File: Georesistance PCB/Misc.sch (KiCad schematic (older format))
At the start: 20 parts, among them J1 Screw_Terminal_01x04, J2 Screw_Terminal_01x02, J3 Conn_01x11_Male, U1 RS8554, U5 TXS0108EPWR, U7 ADS1115IDGS

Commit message: Actually fixed the schematic
Hopefully for the last time
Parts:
- renumbered U7 to U6
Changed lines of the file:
@@
 	9650 1500 9350 1500
 $Comp
-L Analog_ADC:ADS1115IDGS U7
+L Analog_ADC:ADS1115IDGS U6
 U 1 1 613ED4C8
 P 9350 2000
-F 0 "U7" H 9350 2681 50  0001 C CNN
+F 0 "U6" H 9350 2681 50  0001 C CNN
 F 1 "ADS1115IDGS" H 9350 2590 50  0001 C CNN
 F 2 "Package_SO:TSSOP-10_3x3mm_P0.5mm" H 9350 1500 50  0001 C CNN

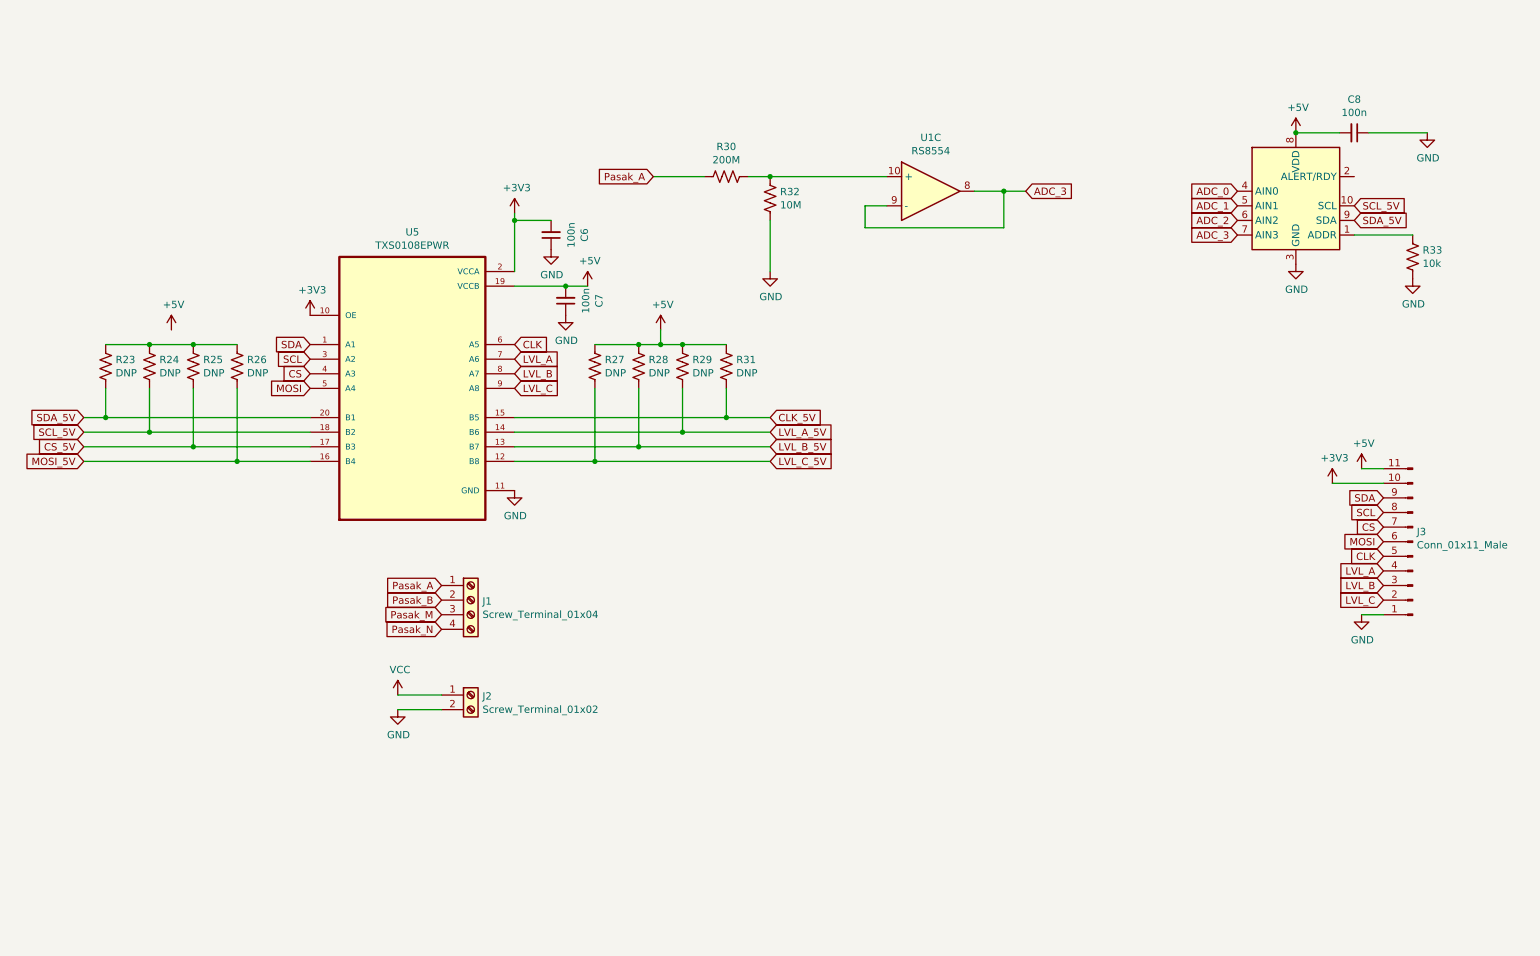
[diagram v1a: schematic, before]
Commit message: Added the PCB layout and simplified schematic
deleted jumper, and fixed misconnection
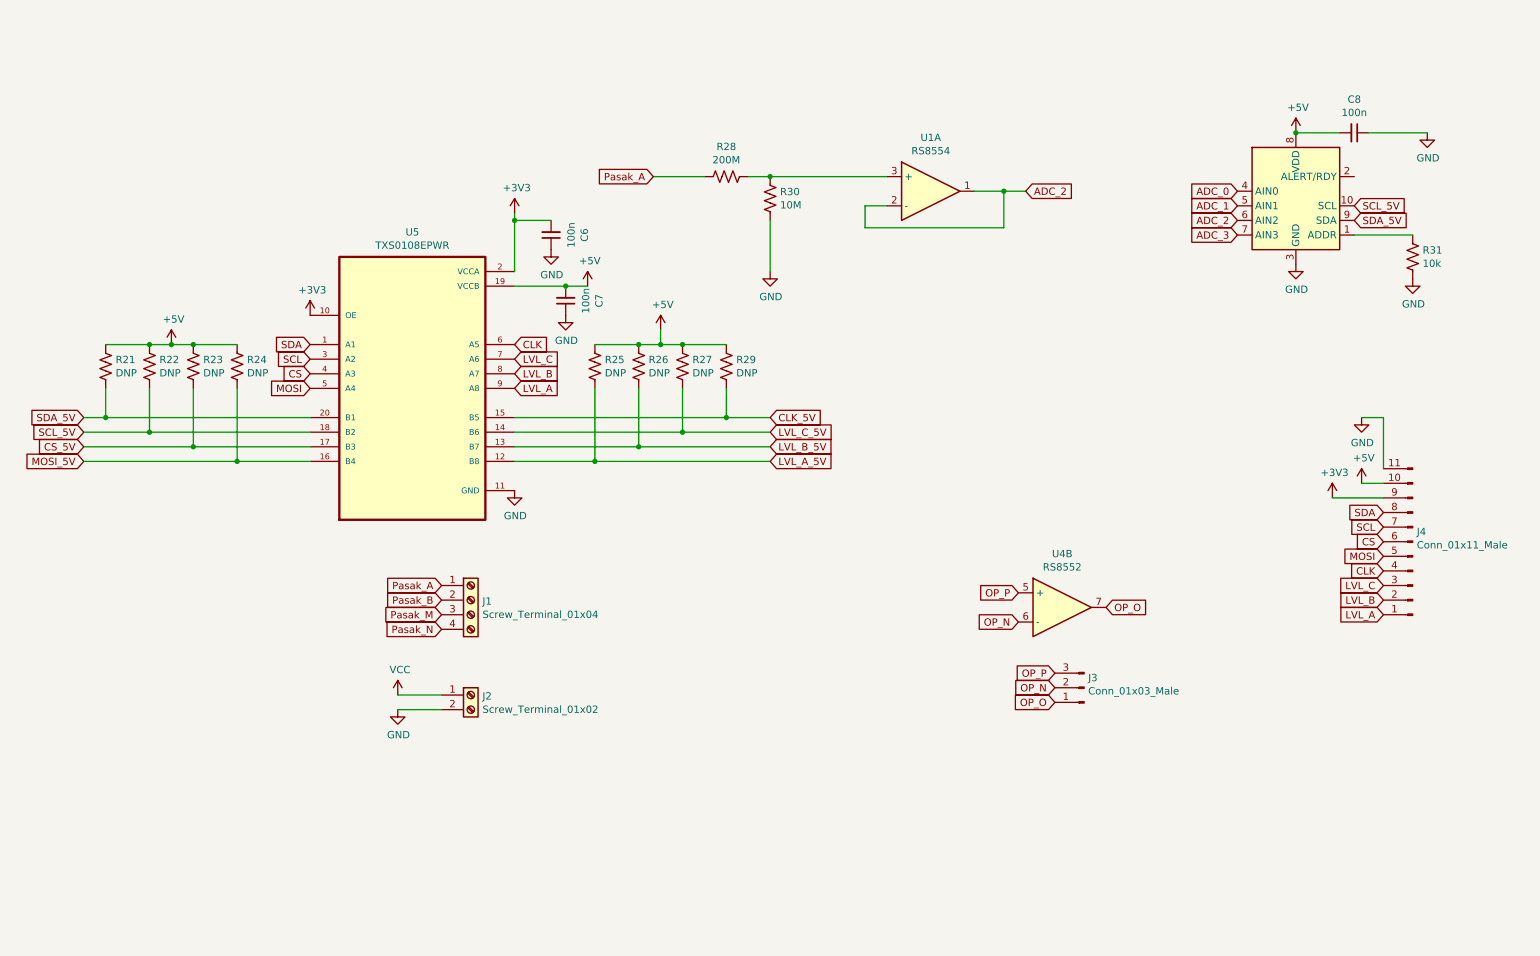
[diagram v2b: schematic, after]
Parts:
- added J3: Conn_01x03_Male, Connector_PinSocket_2.54mm:PinSocket_1x03_P2.54mm_Vertical, symbol Connector:Conn_01x03_Male
- added U4: RS8552, Package_SO:MSOP-8_3x3mm_P0.65mm, symbol Device:Opamp_Dual_Generic
- renumbered J3 to J4, R23 to R21, R24 to R22, R25 to R23, R26 to R24, R27 to R25, R28 to R26, R29 to R27, R30 to R28, R31 to R29, R32 to R30, R33 to R31
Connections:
- net +3V3: now also J4.9 (Pin_9); no longer J4.10 (Pin_10)
- net +5V: now also J4.10 (Pin_10), R21.1, R22.1, R23.1, R24.1; no longer J4.11 (Pin_11)
- net ADC_2: now also U1.1, U1.2 (-)
- net ADC_3: no longer U1.8, U1.9 (-)
- net CLK: now also J4.4 (Pin_4); no longer J4.5 (Pin_5)
- net CS: now also J4.6 (Pin_6); no longer J4.7 (Pin_7)
- net GND: now also J4.11 (Pin_11); no longer J4.1 (Pin_1)
- net LVL_A: now also J4.1 (Pin_1), U5.9 (A8); no longer J4.4 (Pin_4), U5.7 (A6)
- net LVL_A_5V: now also R25.2, U5.12 (B8); no longer R27.2, U5.14 (B6)
- net LVL_B: now also J4.2 (Pin_2); no longer J4.3 (Pin_3)
- net LVL_C: now also J4.3 (Pin_3), U5.7 (A6); no longer J4.2 (Pin_2), U5.9 (A8)
- net LVL_C_5V: now also R27.2, U5.14 (B6); no longer R25.2, U5.12 (B8)
- net MOSI: now also J4.5 (Pin_5); no longer J4.6 (Pin_6)
- net SCL: now also J4.7 (Pin_7); no longer J4.8 (Pin_8)
- net SDA: now also J4.8 (Pin_8); no longer J4.9 (Pin_9)
- net at R28.1, R30.2: now also U1.3 (+); no longer U1.10 (+)
- new net OP_N: J3.2 (Pin_2), U4.6 (-)
- new net OP_O: J3.1 (Pin_1), U4.7
- new net OP_P: J3.3 (Pin_3), U4.5 (+)

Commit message: added things
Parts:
- added H1, H2, H3, H4: MountingHole, MountingHole:MountingHole_3.2mm_M3_DIN965, symbol Mechanical:MountingHole
- U5: value TXS0108EPWR -> RS0108
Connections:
- no-connect marks 0 -> 1
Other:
- moved on the sheet: C6, C7, C8, J1, J2, J3, J4, R21, R22, R23, R24, R25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
